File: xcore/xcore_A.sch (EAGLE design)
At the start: 77 parts, among them J0 LIWE_40_PIN, U1 NC7WZ07, U2 FIN1002, U3 FIN1002, X0D11 TPTP14R, X1 XEF216-512-TQ128, X1D00 TPTP14R

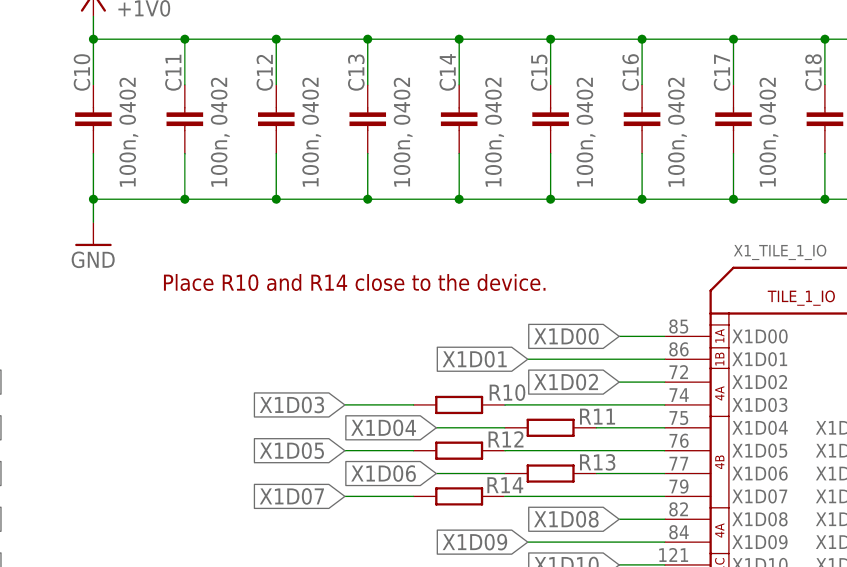
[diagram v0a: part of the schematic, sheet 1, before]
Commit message: xcore: updated with new 3x con symbol names
Signed-off-by: malo <pavol.malosek@gmail.com>
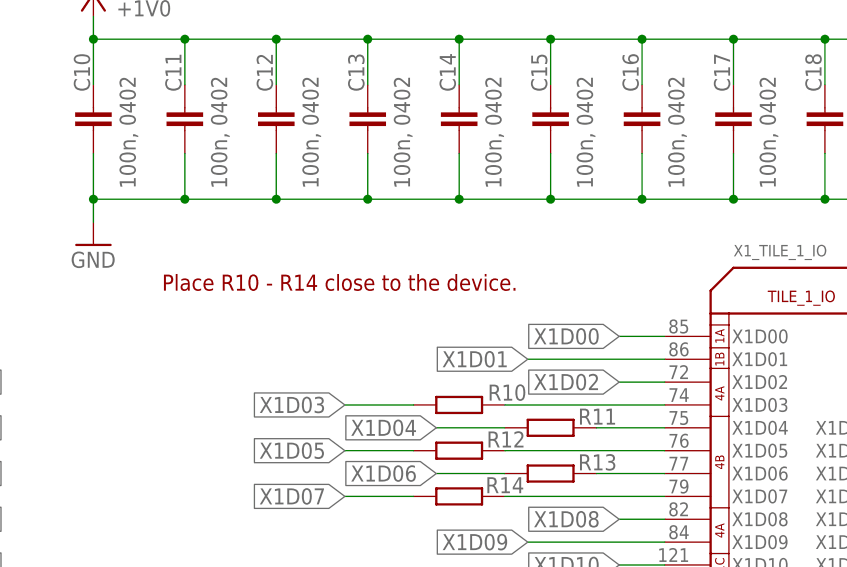
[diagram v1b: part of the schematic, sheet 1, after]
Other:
- note added: "Place R10 - R14 close to the device."
- note removed: "Place R10 and R14 close to the device."
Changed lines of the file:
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@@
 <text x="342.9" y="20.32" size="2.54" layer="94">http://25cmsquare.io</text>
 <text x="73.66" y="66.04" size="1.778" layer="94">Place R4 and R5 close to the device.</text>
-<text x="195.58" y="180.34" size="1.778" layer="94">Place R10 and R14 close to the device.</text>
+<text x="195.58" y="180.34" size="1.778" layer="94">Place R10 - R14 close to the device.</text>
 </plain>
 <instances>

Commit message: xcore: added differential I/O for x0d38 and x0d39 (spdif I/O)
Signed-off-by: malo <pavol.malosek@gmail.com>
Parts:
- added C5, C6: 100n, 0603, rcl:C-EUC0603
- added R30, R31, R32, R33: (no value), rcl:R-EU_R0603
- added U4: FIN1002, 25cmsquare:FIN1002
- added U5: FIN1001, 25cmsquare:FIN1001
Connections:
- new net N$10: R32.1, U5.ROUT+
- new net N$11: R33.1, U5.ROUT-
- new net N$6: R30.1, U4.ROUT
- new net N$7: R31.2, U5.RIN
- new net X0D38_N: J_TO_MASTER.39, U4.RIN-
- new net X0D38_P: J_TO_MASTER.37, U4.RIN+
- new net X0D39_N: J_TO_MASTER.43, R33.2
- new net X0D39_P: J_TO_MASTER.45, R32.2
- net +3V3: now also C5.2, C6.2, U4.VCC, U5.VCC
- net GND: now also C5.1, C6.1, U4.GND, U5.GND
- net X0D36: now also J_TO_MASTER.36; no longer J_TO_MASTER.39
- net X0D38: now also R30.2; no longer J_TO_MASTER.42
- net X0D39: now also R31.1; no longer J_TO_MASTER.43
- net X1D10: now also J_TO_MASTER.33; no longer J_TO_MASTER.36
- net X1D11: now also J_TO_MASTER.34; no longer J_TO_MASTER.37
- net X1D26: now also J_TO_MASTER.21; no longer J_TO_MASTER.24
- net X1D27: now also J_TO_MASTER.22; no longer J_TO_MASTER.25
- net X1D28: now also J_TO_MASTER.24; no longer J_TO_MASTER.27
- net X1D29: now also J_TO_MASTER.25; no longer J_TO_MASTER.28
- net X1D30: now also J_TO_MASTER.27; no longer J_TO_MASTER.30
- net X1D31: now also J_TO_MASTER.28; no longer J_TO_MASTER.31
- net X1D32: now also J_TO_MASTER.30; no longer J_TO_MASTER.33
- net X1D33: now also J_TO_MASTER.31; no longer J_TO_MASTER.34
- net X1D35: now also J_TO_MASTER.42; no longer J_TO_MASTER.45
- net X1D40: now also J_TO_MASTER.9; no longer J_TO_MASTER.18
- net X1D41: now also J_TO_MASTER.16; no longer J_TO_MASTER.19
- net X1D42: now also J_TO_MASTER.18; no longer J_TO_MASTER.21
- net X1D43: now also J_TO_MASTER.19; no longer J_TO_MASTER.22
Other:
- note removed: "This work is licensed under a Creative Commons Attribution-ShareAlike 4.0 International License. http://creativecommons.org/licenses/by-sa/4.0/"
- note removed: "http://25cmsquare.io"
- moved on the sheet: C2, JP1, JP2, J_TO_SLAVE, R10, R11, R12, R13, R14, R27, R28, U2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
